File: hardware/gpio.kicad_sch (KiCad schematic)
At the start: 3 parts, among them U2 W65C22SxP, U4 W65C22SxP, U5 74AHC1G04

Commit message: Improved labels
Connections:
- net GPIO_CS renamed GPIO_{CS}
- net IRQ1 renamed IRQ_{1}
- net IRQ_{1}: no longer U4.21 (~{IRQ})
- new net IRQ_{2}: U4.21 (~{IRQ})

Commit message: Improved Schematics and added fooprints
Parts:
- U5: footprint (none) -> Package_TO_SOT_SMD:SOT-23-5
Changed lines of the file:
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@@
+		)
+	)
+	(wire
+		(pts
+			(xy 205.74 77.47) (xy 213.36 77.47)
+		)
+		(stroke
+			(width 0)
+			(type default)
 		)
 	)
@@
 	(wire
 		(pts
-			(xy 132.08 85.09) (xy 140.97 85.09)
+			(xy 132.08 85.09) (xy 139.7 85.09)
 		)
 		(stroke
@@
 	)
 	(global_label "PORT_CC1"
-		(shape input)
+		(shape output)
 		(at 215.9 82.55 0)
 		(fields_autoplaced yes)
@@
 	)
 	(global_label "PORT_CA1"
-		(shape input)
+		(shape output)
 		(at 139.7 82.55 0)
 		(fields_autoplaced yes)
@@
 			)
 		)
-		(property "Footprint" ""
+		(property "Footprint" "Package_TO_SOT_SMD:SOT-23-5"
 			(at 186.69 30.48 0)
 			(effects
@@
 	)
 	(symbol
+		(lib_name "W65C22SxP_1")
 		(lib_id "65xx-library:W65C22SxP")
 		(at 121.92 90.17 0)

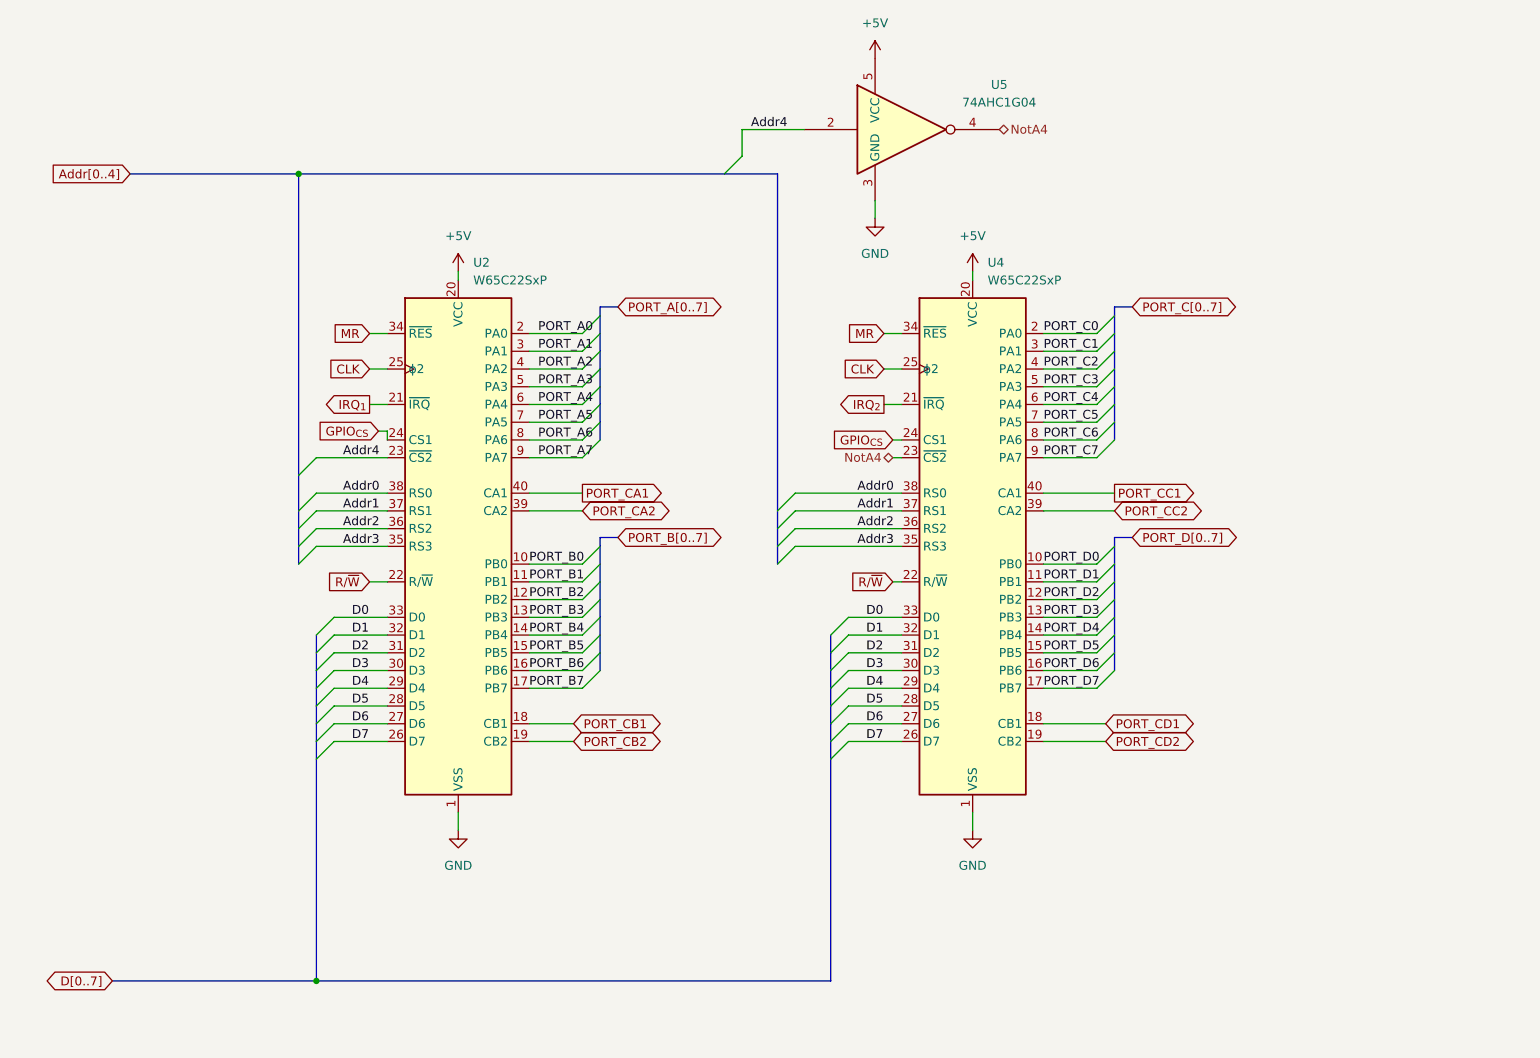
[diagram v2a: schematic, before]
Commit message: Added Clock and Ethernet via SPI
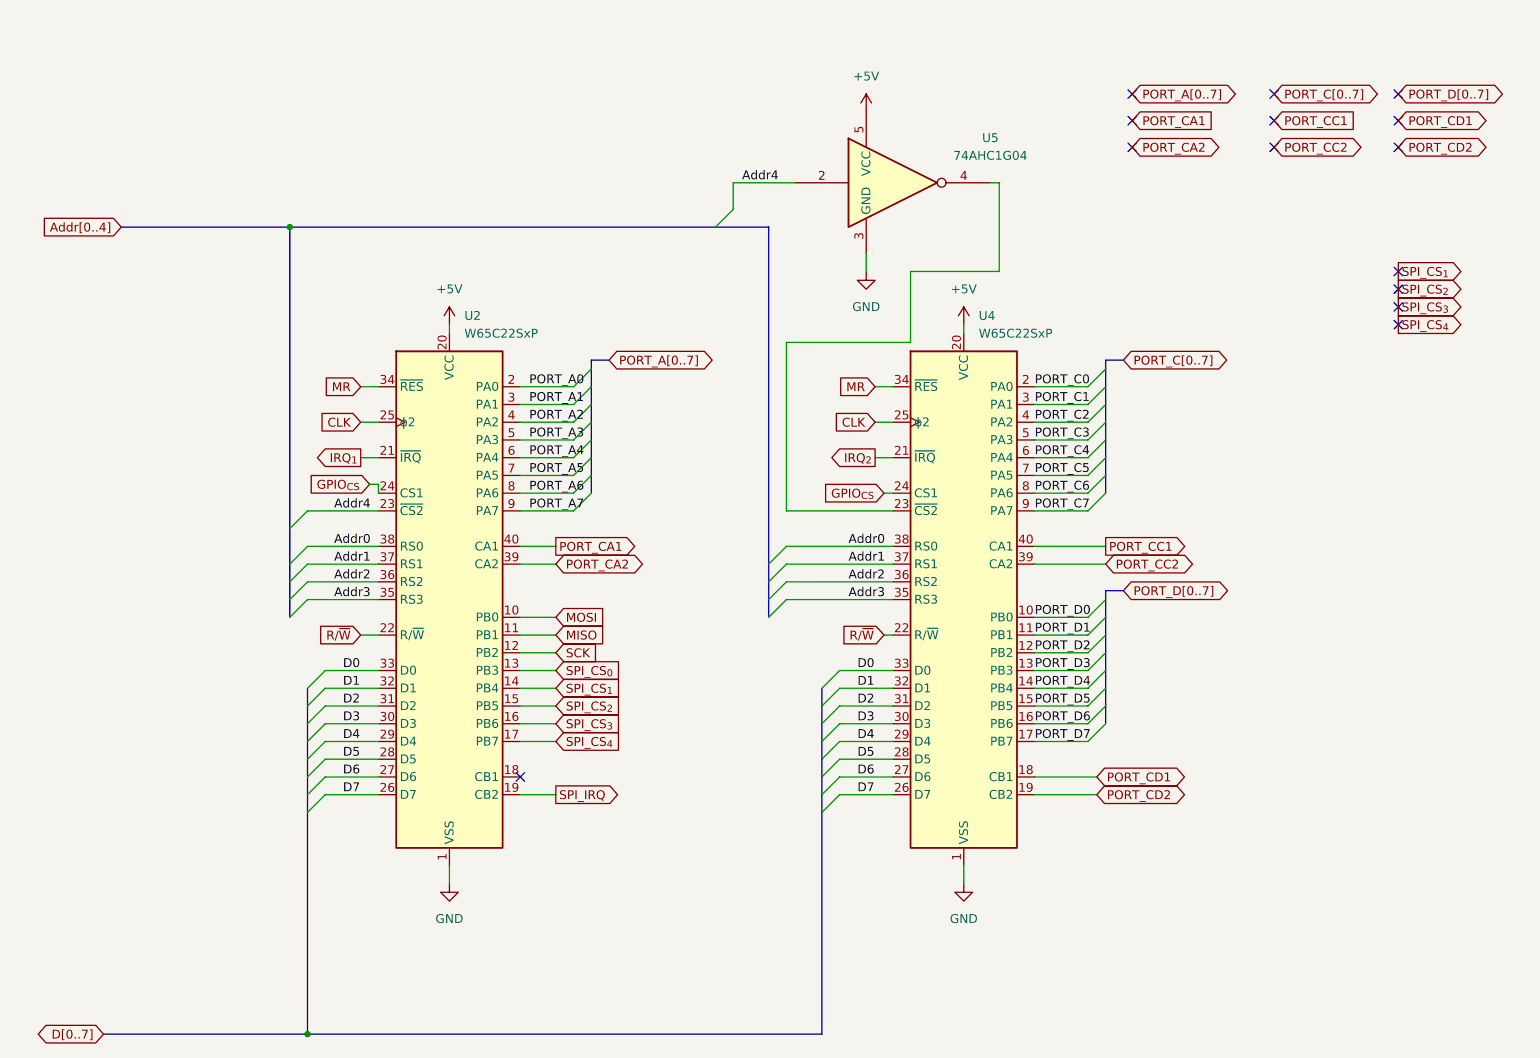
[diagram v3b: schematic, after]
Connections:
- net NotA4: no longer names the net of U4.23 (~{CS2}), U5.4
- net PORT_B0 renamed MOSI
- net PORT_B1 renamed MISO
- net PORT_B2 renamed SCK
- net PORT_B3 renamed SPI_CS_{0}
- net PORT_B4 renamed SPI_CS_{1}
- net PORT_B5 renamed SPI_CS_{2}
- net PORT_B6 renamed SPI_CS_{3}
- net PORT_B7 renamed SPI_CS_{4}
- net PORT_CB1: no longer names the net of U2.18 (CB1)
- net PORT_CB2 renamed SPI_IRQ
- no-connect marks 0 -> 14
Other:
- moved on the sheet: U2, U4, U5

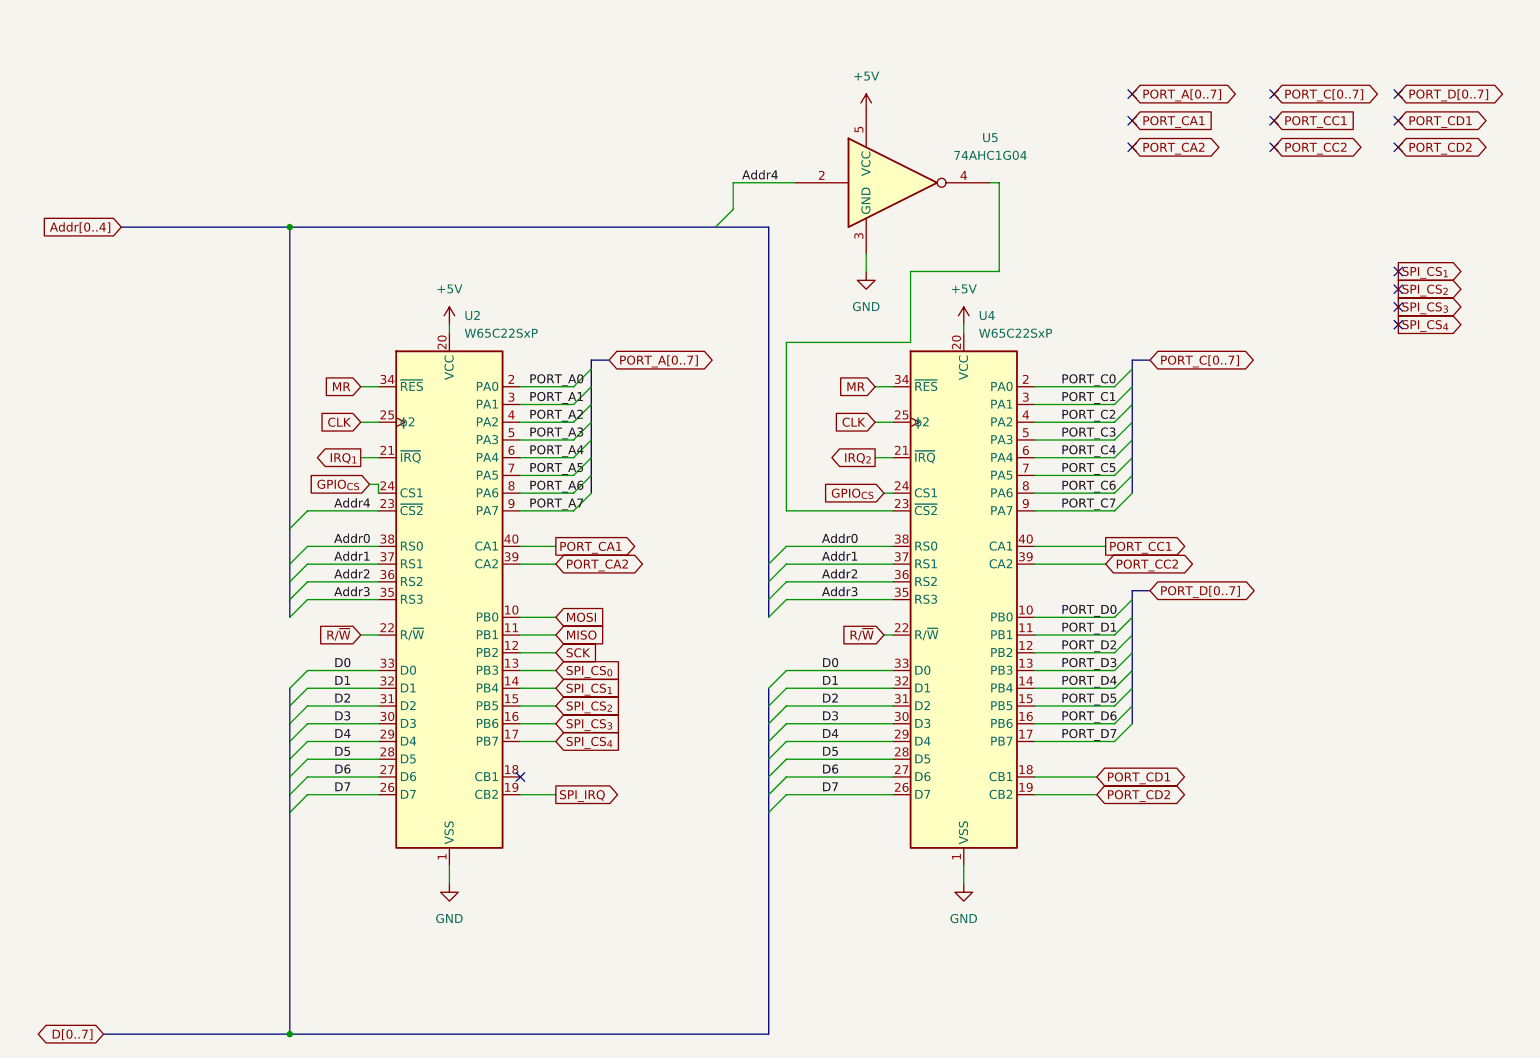
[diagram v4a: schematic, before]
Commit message: Added External connectors
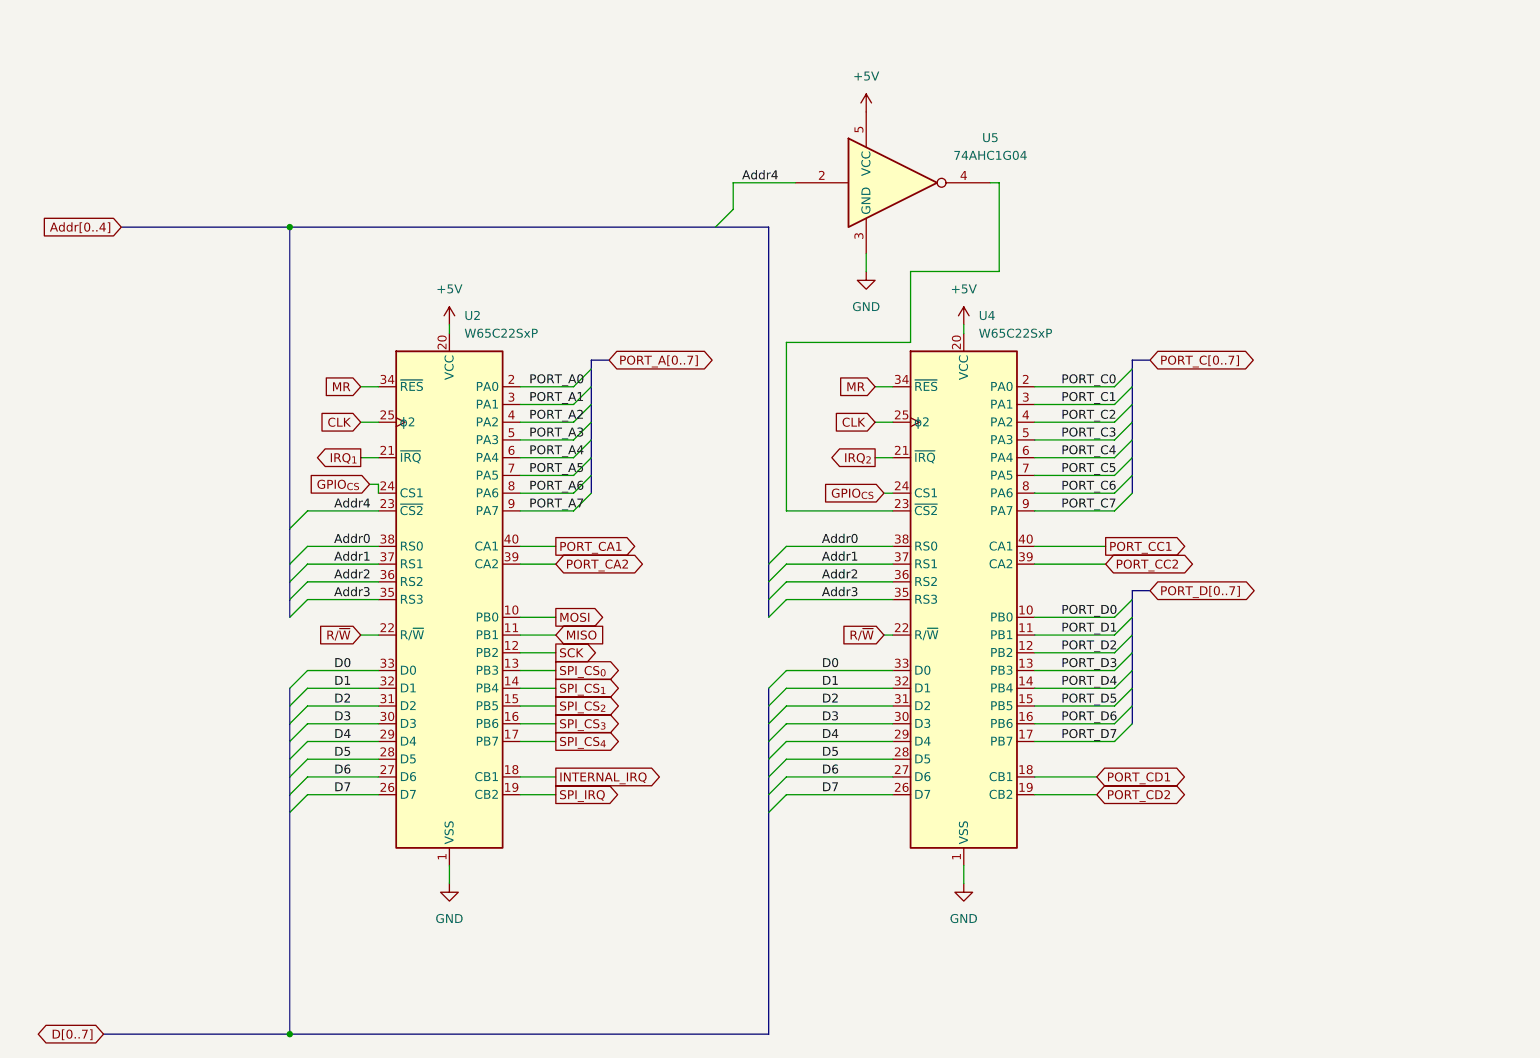
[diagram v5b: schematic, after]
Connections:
- net INTERNAL_IRQ: now reaches U2.18 (CB1)
- no-connect marks 14 -> 0

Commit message: Fixed some erros, changed to 3V
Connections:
- net +5V renamed +3.3V
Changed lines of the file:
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@@
 	)
 	(symbol
-		(lib_id "power:+5V")
+		(lib_id "power:+3.3V")
+		(at 120.65 58.42 0)
+		(unit 1)
+		(exclude_from_sim no)
+		(in_bom yes)
+		(on_board yes)
+		(dnp no)
+		(property "Reference" "#PWR05"
+			(at 120.65 62.23 0)
+			(effects
+				(font
+					(size 1.27 1.27)
+				)
+				(hide yes)
+			)
+		)
+		(property "Value" "+3.3V"
+			(at 120.65 53.34 0)
+			(effects
+				(font
+					(size 1.27 1.27)
+				)
+			)
+		)
+		(property "Footprint" ""
+			(at 120.65 58.42 0)
+			(effects
+				(font
+					(size 1.27 1.27)
+				)
+				(hide yes)
+			)
+		)
+		(property "Datasheet" ""
+			(at 120.65 58.42 0)
+			(effects
+				(font
+					(size 1.27 1.27)
+				)
+				(hide yes)
+			)
+		)
+		(property "Description" "Power symbol creates a global label with name \"+3.3V\""
+			(at 120.65 58.42 0)
+			(effects
+				(font
+					(size 1.27 1.27)
+				)
+				(hide yes)
+			)
+		)
+		(pin "1"
+		)
+		(instances
+			(project "Lambda One"
+				(path "/73ea9964-373f-4fdc-b03e-f532cf836c0d/c99586b2-79bd-4011-9acf-fcc28a8dd9c0"
+					(reference "#PWR05")
+					(unit 1)
+				)
+			)
+		)
+	)
+	(symbol
+		(lib_id "power:+3.3V")
 		(at 194.31 58.42 0)
 		(unit 1)
@@
 		(on_board yes)
 		(dnp no)
-		(fields_autoplaced yes)
 		(property "Reference" "#PWR06"
 			(at 194.31 62.23 0)
@@
 			)
 		)
-		(property "Value" "+5V"
+		(property "Value" "+3.3V"
 			(at 194.31 53.34 0)
 			(effects
@@
 			)
 		)
-		(property "Description" "Power symbol creates a global label with name \"+5V\""
+		(property "Description" "Power symbol creates a global label with name \"+3.3V\""
 			(at 194.31 58.42 0)
 			(effects
@@
 	)
 	(symbol
+		(lib_id "power:+3.3V")
+		(at 180.34 27.94 0)
+		(unit 1)
+		(exclude_from_sim no)
+		(in_bom yes)
+		(on_board yes)
+		(dnp no)
+		(property "Reference" "#PWR09"
+			(at 180.34 31.75 0)
+			(effects
+				(font
+					(size 1.27 1.27)
+				)
+				(hide yes)
+			)
+		)
+		(property "Value" "+3.3V"
+			(at 180.34 22.86 0)
+			(effects
+				(font
+					(size 1.27 1.27)
+				)
+			)
+		)
+		(property "Footprint" ""
+			(at 180.34 27.94 0)
+			(effects
+				(font
+					(size 1.27 1.27)
+				)
+				(hide yes)
+			)
+		)
+		(property "Datasheet" ""
+			(at 180.34 27.94 0)
+			(effects
+				(font
+					(size 1.27 1.27)
+				)
+				(hide yes)
+			)
+		)
+		(property "Description" "Power symbol creates a global label with name \"+3.3V\""
+			(at 180.34 27.94 0)
+			(effects
+				(font
+					(size 1.27 1.27)
+				)
+				(hide yes)
+			)
+		)
+		(pin "1"
+		)
+		(instances
+			(project "Lambda One"
+				(path "/73ea9964-373f-4fdc-b03e-f532cf836c0d/c99586b2-79bd-4011-9acf-fcc28a8dd9c0"
+					(reference "#PWR09")
+					(unit 1)
+				)
+			)
+		)
+	)
+	(symbol
 		(lib_id "power:GND")
 		(at 180.34 50.8 0)
@@
 	)
 	(symbol
-		(lib_id "power:+5V")
-		(at 120.65 58.42 0)
-		(unit 1)
-		(exclude_from_sim no)
-		(in_bom yes)
-		(on_board yes)
-		(dnp no)
-		(fields_autoplaced yes)
-		(property "Reference" "#PWR05"
-			(at 120.65 62.23 0)
-			(effects
-				(font
-					(size 1.27 1.27)
-				)
-				(hide yes)
-			)
-		)
-		(property "Value" "+5V"
-			(at 120.65 53.34 0)
-			(effects
-				(font
-					(size 1.27 1.27)
-				)
-			)
-		)
-		(property "Footprint" ""
-			(at 120.65 58.42 0)
-			(effects
-				(font
-					(size 1.27 1.27)
-				)
-				(hide yes)
-			)
-		)
-		(property "Datasheet" ""
-			(at 120.65 58.42 0)
-			(effects
-				(font
-					(size 1.27 1.27)
-				)
-				(hide yes)
-			)
-		)
-		(property "Description" "Power symbol creates a global label with name \"+5V\""
-			(at 120.65 58.42 0)
-			(effects
-				(font
-					(size 1.27 1.27)
-				)
-				(hide yes)
-			)
-		)
-		(pin "1"
-		)
-		(instances
-			(project "Lambda One"
-				(path "/73ea9964-373f-4fdc-b03e-f532cf836c0d/c99586b2-79bd-4011-9acf-fcc28a8dd9c0"
-					(reference "#PWR05")
-					(unit 1)
-				)
-			)
-		)
-	)
-	(symbol
 		(lib_id "power:GND")
 		(at 120.65 138.43 0)
@@
 					(unit 1)
 				)
-			)
-		)
-	)
-	(symbol
-		(lib_id "power:+5V")
-		(at 180.34 27.94 0)
-		(unit 1)
-		(exclude_from_sim no)
-		(in_bom yes)
-		(on_board yes)
-		(dnp no)
-		(fields_autoplaced yes)
-		(property "Reference" "#PWR09"
-			(at 180.34 31.75 0)
-			(effects
-				(font
-					(size 1.27 1.27)
-				)
-				(hide yes)
-			)
-		)
-		(property "Value" "+5V"
-			(at 180.34 22.86 0)
-			(effects
-				(font
-					(size 1.27 1.27)
-				)
-			)
-		)
-		(property "Footprint" ""
-			(at 180.34 27.94 0)
-			(effects
-				(font
-					(size 1.27 1.27)
-				)
-				(hide yes)
-			)
-		)
-		(property "Datasheet" ""
-			(at 180.34 27.94 0)
-			(effects
-				(font
-					(size 1.27 1.27)
-				)
-				(hide yes)
-			)
-		)
-		(property "Description" "Power symbol creates a global label with name \"+5V\""
-			(at 180.34 27.94 0)
-			(effects
-				(font
-					(size 1.27 1.27)
-				)
-				(hide yes)
-			)
-		)
-		(pin "1"
-		)
-		(instances
-			(project "Lambda One"
-				(path "/73ea9964-373f-4fdc-b03e-f532cf836c0d/c99586b2-79bd-4011-9acf-fcc28a8dd9c0"
-					(reference "#PWR09")
-					(unit 1)
-				)

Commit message: Fixed all erros and warning
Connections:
- net IRQ_{2} is gone; now on net ~{IRQ}: U4.21 (~{IRQ})
- net IRQ_{1} renamed ~{IRQ}
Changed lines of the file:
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@@
 		)
 	)
-	(global_label "IRQ_{1}"
+	(global_label "~{IRQ}"
 		(shape output)
 		(at 107.95 77.47 180)
@@
 		)
 		(property "Intersheetrefs" "${INTERSHEET_REFS}"
-			(at 100.7411 77.47 0)
+			(at 101.7595 77.47 0)
 			(effects
 				(font
@@
 		)
 	)
-	(global_label "IRQ_{2}"
+	(global_label "~{IRQ}"
 		(shape output)
 		(at 181.61 77.47 180)
@@
 		)
 		(property "Intersheetrefs" "${INTERSHEET_REFS}"
-			(at 174.4011 77.47 0)
+			(at 175.4195 77.47 0)
 			(effects
 				(font

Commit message: Fixed critical bugs on the system related to memory maping and IC selections
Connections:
- net CLK renamed PHI2
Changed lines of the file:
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@@
-		)
-	)
-	(global_label "CLK"
-		(shape input)
-		(at 181.61 72.39 180)
-		(fields_autoplaced yes)
-		(effects
-			(font
-				(size 1.27 1.27)
-			)
-			(justify right)
-		)
-		(property "Intersheetrefs" "${INTERSHEET_REFS}"
-			(at 175.0567 72.39 0)
-			(effects
-				(font
-					(size 1.27 1.27)
-				)
-				(justify right)
-				(hide yes)
-			)
 		)
 	)
@@
 		(property "Intersheetrefs" "${INTERSHEET_REFS}"
 			(at 100.9129 102.87 0)
+			(effects
+				(font
+					(size 1.27 1.27)
+				)
+				(justify right)
+				(hide yes)
+			)
+		)
+	)
+	(global_label "PHI2"
+		(shape input)
+		(at 107.95 72.39 180)
+		(fields_autoplaced yes)
+		(effects
+			(font
+				(size 1.27 1.27)
+			)
+			(justify right)
+		)
+		(property "Intersheetrefs" "${INTERSHEET_REFS}"
+			(at 100.55 72.39 0)
 			(effects
 				(font
@@
 		)
 	)
-	(global_label "CLK"
-		(shape input)
-		(at 107.95 72.39 180)
-		(fields_autoplaced yes)
-		(effects
-			(font
-				(size 1.27 1.27)
-			)
-			(justify right)
-		)
-		(property "Intersheetrefs" "${INTERSHEET_REFS}"
-			(at 101.3967 72.39 0)
-			(effects
-				(font
-					(size 1.27 1.27)
-				)
-				(justify right)
-				(hide yes)
-			)
-		)
-	)
 	(global_label "PORT_CA2"
 		(shape bidirectional)
@@
 				(hide yes)
 			)
+		)
+	)
+	(global_label "PHI2"
+		(shape input)
+		(at 181.61 72.39 180)
+		(fields_autoplaced yes)
+		(effects
+			(font
+				(size 1.27 1.27)
+			)
+			(justify right)
+		)
+		(property "Intersheetrefs" "${INTERSHEET_REFS}"
+			(at 174.21 72.39 0)
+			(effects
+				(font
+					(size 1.27 1.27)
+				)
+				(justify right)
+				(hide yes)
+			)
